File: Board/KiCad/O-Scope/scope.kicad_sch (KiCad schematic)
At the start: 50 parts, among them U4 MCP6021, U5 MCP6N11-001E_SN, U6 MCP6N11-001E_SN, U7 MCP6024, U8 CD74HC4053

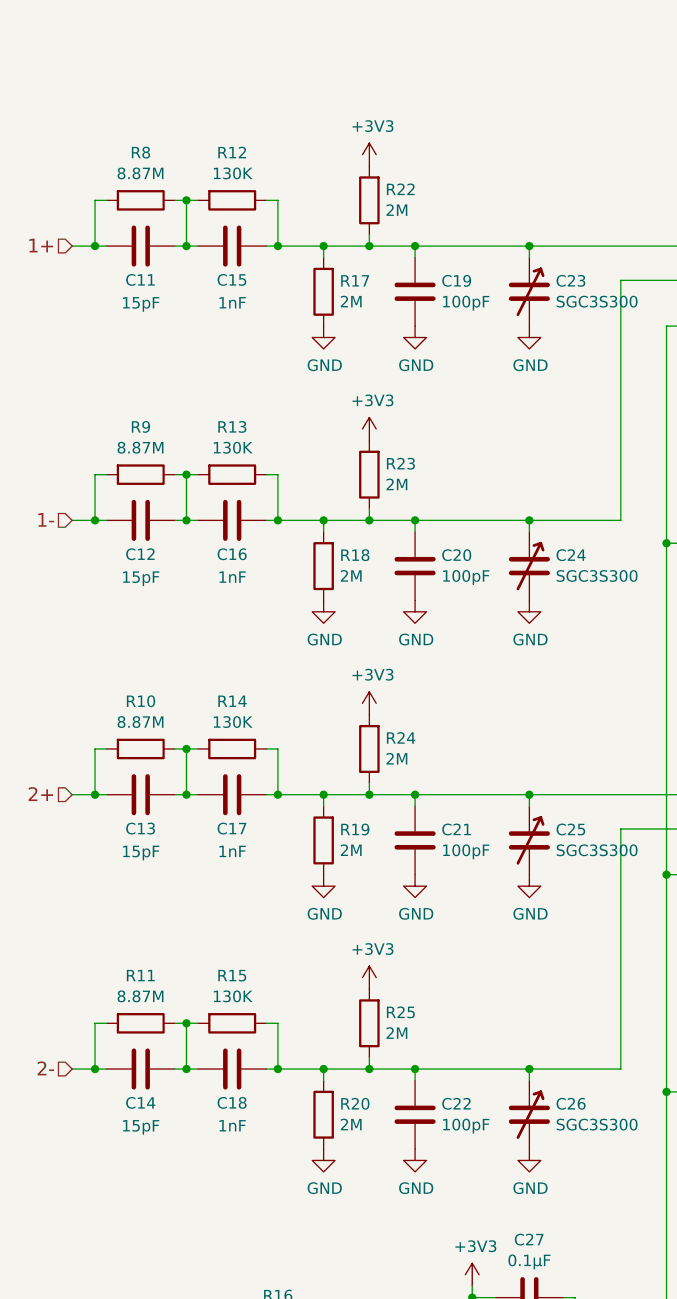
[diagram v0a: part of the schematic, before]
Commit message: Fixed scope probe input resistive divider values to match current O-Scopes (i.e. 1 MΩ input resistance instead of 10 MΩ).
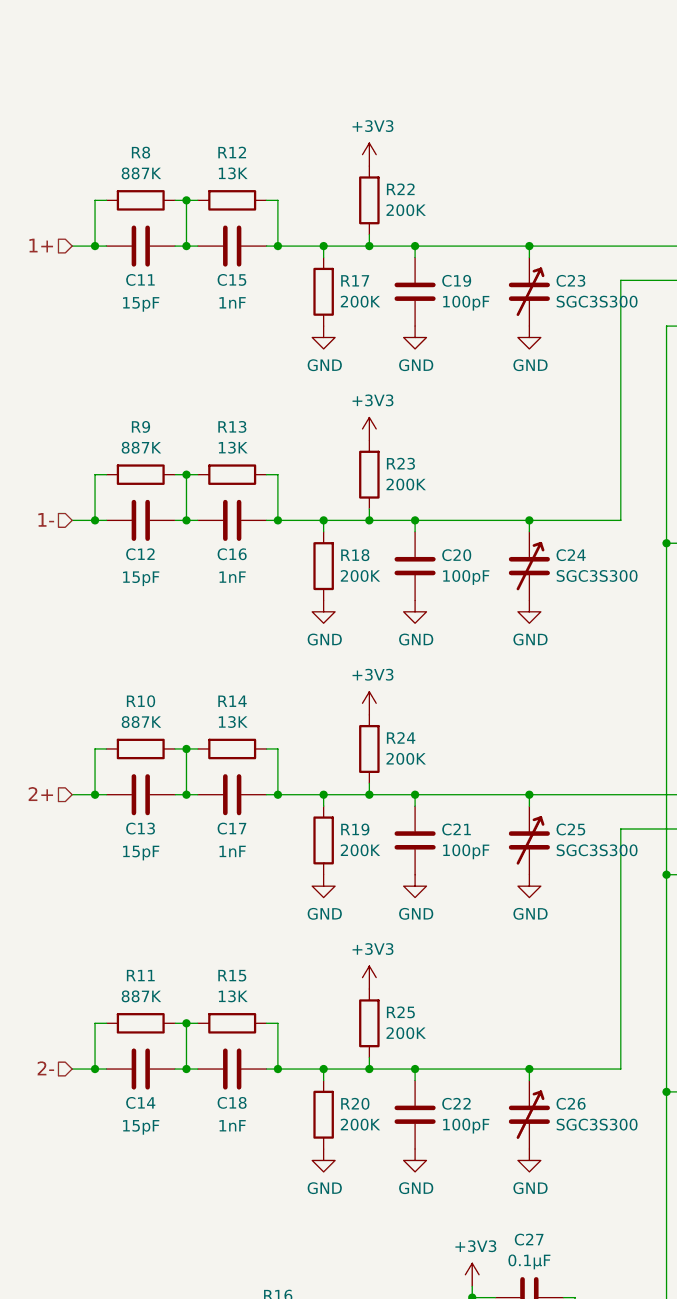
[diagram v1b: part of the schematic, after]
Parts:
- R10, R11, R8, R9: value 8.87M -> 887K
- R12, R13, R14, R15: value 130K -> 13K
- R17, R18, R19, R20, R22, R23, R24, R25: value 2M -> 200K
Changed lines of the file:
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@@
     (in_bom yes) (on_board yes)
     (property "Reference" "R8" (id 0) (at 128.27 69.6722 90))
-    (property "Value" "8.87M" (id 1) (at 128.27 71.9836 90))
+    (property "Value" "887K" (id 1) (at 128.27 71.9836 90))
     (property "Footprint" "Resistor_SMD:R_0805_2012Metric" (id 2) (at 128.27 73.152 90)
       (effects (font (size 1.27 1.27)) hide)
@@
     (in_bom yes) (on_board yes)
     (property "Reference" "R12" (id 0) (at 138.43 69.6722 90))
-    (property "Value" "130K" (id 1) (at 138.43 71.9836 90))
+    (property "Value" "13K" (id 1) (at 138.43 71.9836 90))
     (property "Footprint" "Resistor_SMD:R_0603_1608Metric" (id 2) (at 138.43 73.152 90)
       (effects (font (size 1.27 1.27)) hide)
@@
       (effects (font (size 1.27 1.27)) (justify right))
     )
-    (property "Value" "2M" (id 1) (at 155.448 76.073 0)
+    (property "Value" "200K" (id 1) (at 155.448 76.073 0)
       (effects (font (size 1.27 1.27)) (justify right))
     )
@@
       (effects (font (size 1.27 1.27)) (justify right))
     )
-    (property "Value" "2M" (id 1) (at 150.368 86.233 0)
+    (property "Value" "200K" (id 1) (at 150.368 86.233 0)
       (effects (font (size 1.27 1.27)) (justify right))
     )
@@
     (in_bom yes) (on_board yes)
     (property "Reference" "R9" (id 0) (at 128.27 100.1522 90))
-    (property "Value" "8.87M" (id 1) (at 128.27 102.4636 90))
+    (property "Value" "887K" (id 1) (at 128.27 102.4636 90))
     (property "Footprint" "Resistor_SMD:R_0805_2012Metric" (id 2) (at 128.27 103.632 90)
       (effects (font (size 1.27 1.27)) hide)
@@
     (in_bom yes) (on_board yes)
     (property "Reference" "R13" (id 0) (at 138.43 100.1522 90))
-    (property "Value" "130K" (id 1) (at 138.43 102.4636 90))
+    (property "Value" "13K" (id 1) (at 138.43 102.4636 90))
     (property "Footprint" "Resistor_SMD:R_0603_1608Metric" (id 2) (at 138.43 103.632 90)
       (effects (font (size 1.27 1.27)) hide)
@@
       (effects (font (size 1.27 1.27)) (justify right))
     )
-    (property "Value" "2M" (id 1) (at 155.448 106.553 0)
+    (property "Value" "200K" (id 1) (at 155.448 106.553 0)
       (effects (font (size 1.27 1.27)) (justify right))
     )
@@
       (effects (font (size 1.27 1.27)) (justify right))
     )
-    (property "Value" "2M" (id 1) (at 150.368 116.713 0)
+    (property "Value" "200K" (id 1) (at 150.368 116.713 0)
       (effects (font (size 1.27 1.27)) (justify right))
     )
@@
     (in_bom yes) (on_board yes)
     (property "Reference" "R10" (id 0) (at 128.27 130.6322 90))
-    (property "Value" "8.87M" (id 1) (at 128.27 132.9436 90))
+    (property "Value" "887K" (id 1) (at 128.27 132.9436 90))
     (property "Footprint" "Resistor_SMD:R_0805_2012Metric" (id 2) (at 128.27 134.112 90)
       (effects (font (size 1.27 1.27)) hide)
@@
     (in_bom yes) (on_board yes)
     (property "Reference" "R14" (id 0) (at 138.43 130.6322 90))
-    (property "Value" "130K" (id 1) (at 138.43 132.9436 90))
+    (property "Value" "13K" (id 1) (at 138.43 132.9436 90))
     (property "Footprint" "Resistor_SMD:R_0603_1608Metric" (id 2) (at 138.43 134.112 90)
       (effects (font (size 1.27 1.27)) hide)
@@
       (effects (font (size 1.27 1.27)) (justify right))
     )
-    (property "Value" "2M" (id 1) (at 155.448 137.033 0)
+    (property "Value" "200K" (id 1) (at 155.448 137.033 0)
       (effects (font (size 1.27 1.27)) (justify right))
     )
@@
       (effects (font (size 1.27 1.27)) (justify right))
     )
-    (property "Value" "2M" (id 1) (at 150.368 147.193 0)
+    (property "Value" "200K" (id 1) (at 150.368 147.193 0)
       (effects (font (size 1.27 1.27)) (justify right))
     )
@@
     (in_bom yes) (on_board yes)
     (property "Reference" "R11" (id 0) (at 128.27 161.1122 90))
-    (property "Value" "8.87M" (id 1) (at 128.27 163.4236 90))
+    (property "Value" "887K" (id 1) (at 128.27 163.4236 90))
     (property "Footprint" "Resistor_SMD:R_0805_2012Metric" (id 2) (at 128.27 164.592 90)
       (effects (font (size 1.27 1.27)) hide)
@@
     (in_bom yes) (on_board yes)
     (property "Reference" "R15" (id 0) (at 138.43 161.1122 90))
-    (property "Value" "130K" (id 1) (at 138.43 163.4236 90))
+    (property "Value" "13K" (id 1) (at 138.43 163.4236 90))
     (property "Footprint" "Resistor_SMD:R_0603_1608Metric" (id 2) (at 138.43 164.592 90)
       (effects (font (size 1.27 1.27)) hide)
@@
       (effects (font (size 1.27 1.27)) (justify right))
     )
-    (property "Value" "2M" (id 1) (at 155.448 167.513 0)
+    (property "Value" "200K" (id 1) (at 155.448 167.513 0)
       (effects (font (size 1.27 1.27)) (justify right))
     )
@@
       (effects (font (size 1.27 1.27)) (justify right))
     )
-    (property "Value" "2M" (id 1) (at 150.368 177.673 0)
-      (effects (font (size 1.27 1.27)) (justify right))
-    )
+    (property "Value" "200K" (id 1) (at 150.368 177.673 0)
+      (effects (font (size 1.27 1.27)) (justify right))
+    )
